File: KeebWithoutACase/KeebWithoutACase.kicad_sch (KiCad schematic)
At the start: 134 parts, among them SW1 SW_Push_45deg, SW10 SW_Push_45deg, SW11 SW_Push_45deg, SW12 SW_Push_45deg, SW13 SW_Push_45deg, SW14 2U, SW15 1.5U, SW16 SW_Push_45deg, SW17 SW_Push_45deg, SW18 SW_Push_45deg, SW19 SW_Push_45deg, SW2 SW_Push_45deg, SW20 SW_Push_45deg, SW21 SW_Push_45deg, SW22 SW_Push_45deg, SW23 SW_Push_45deg, SW24 SW_Push_45deg, SW25 SW_Push_45deg, SW26 SW_Push_45deg, SW27 SW_Push_45deg, SW28 1.5U, SW29 1.75U, SW3 SW_Push_45deg, SW30 2.25U, SW31 SW_Push_45deg, SW32 SW_Push_45deg, SW33 SW_Push_45deg, SW34 SW_Push_45deg, SW35 SW_Push_45deg, SW36 SW_Push_45deg, SW37 SW_Push_45deg, SW38 SW_Push_45deg, SW39 SW_Push_45deg, SW4 SW_Push_45deg, SW40 SW_Push_45deg, SW41 SW_Push_45deg, SW42 SW_Push_45deg, SW43 SW_Push_45deg, SW44 SW_Push_45deg, SW45 SW_Push_45deg, SW46 SW_Push_45deg, SW47 SW_Push_45deg, SW48 SW_Push_45deg, SW49 SW_Push_45deg, SW5 SW_Push_45deg, SW50 SW_Push_45deg, SW51 SW_Push_45deg, SW52 2.75U, SW53 2.25U, SW54 1.25U, SW55 RotaryEncoder, SW56 SW_Push_45deg, SW57 1.25U, SW58 SW_Push_45deg, SW59 SW_Push_45deg, SW6 SW_Push_45deg, SW60 SW_Push_45deg, SW62 1.25U, SW63 SW_Push_45deg, SW64 SW_Push_45deg, SW65 SW_Push_45deg, SW66 SW_Push_45deg, SW67 SW_Push_45deg, SW7 SW_Push_45deg, SW8 SW_Push_45deg, SW9 SW_Push_45deg

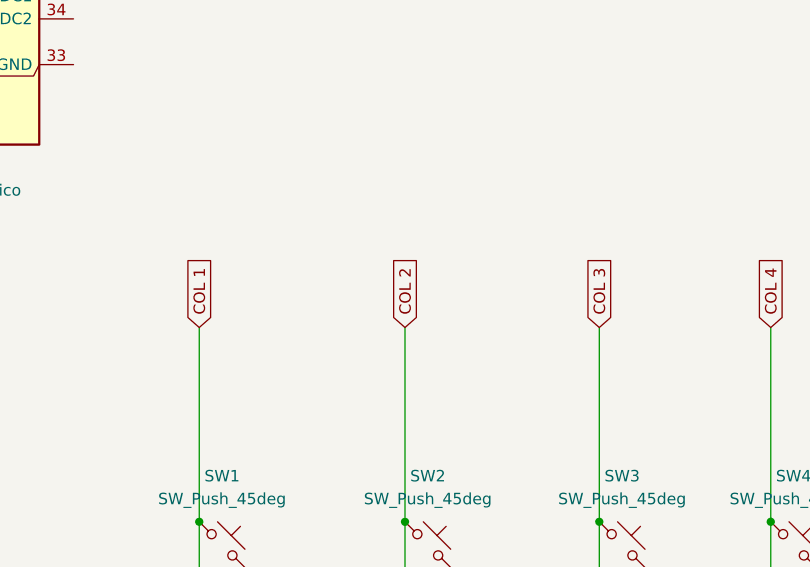
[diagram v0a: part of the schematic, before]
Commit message: this time completed the first row with the correct keys
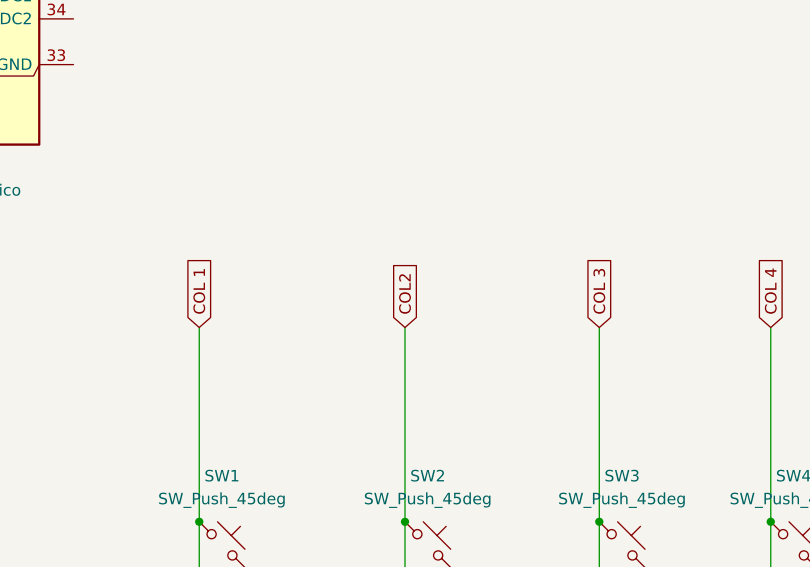
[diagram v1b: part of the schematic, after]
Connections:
- net COL 1: no longer A1.9 (GPIO6)
- new net COL 2: A1.9 (GPIO6)

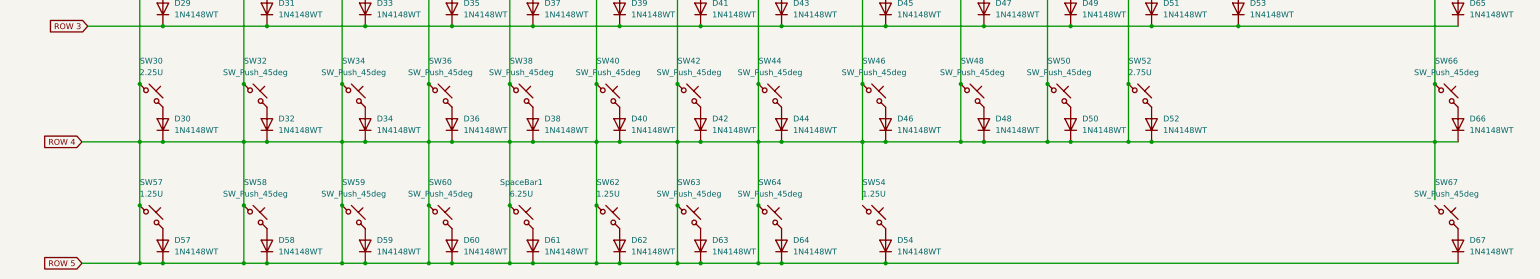
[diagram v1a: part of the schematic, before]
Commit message: fixed the schm col1 bleeding
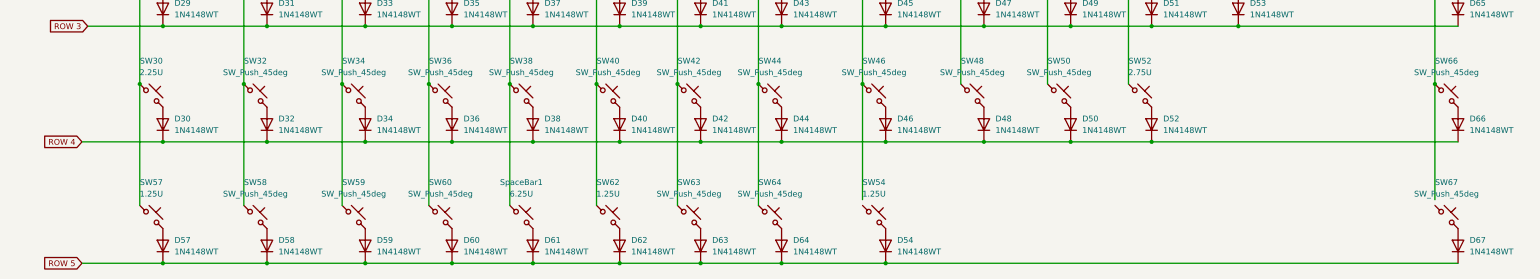
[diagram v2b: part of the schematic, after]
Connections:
- net COL 1: no longer A1.10 (GPIO7), A1.11 (GPIO8), A1.12 (GPIO9), A1.14 (GPIO10), A1.15 (GPIO11), A1.16 (GPIO12), A1.17 (GPIO13), A1.19 (GPIO14), A1.20 (GPIO15), A1.21 (GPIO16), A1.25 (GPIO19), A1.5 (GPIO3), A1.6 (GPIO4), D30.1 (K), D32.1 (K), D34.1 (K), D36.1 (K), D38.1 (K), D40.1 (K), D42.1 (K), D44.1 (K), D46.1 (K), D48.1 (K), D50.1 (K), D52.1 (K), D54.1 (K), D57.1 (K), D58.1 (K), D59.1 (K), D60.1 (K), D61.1 (K), D62.1 (K), D63.1 (K), D64.1 (K), D66.1 (K), D67.1 (K), SW10.1, SW11.1, SW12.1, SW16.1, SW17.1, SW18.1, SW19.1, SW2.1, SW20.1, SW21.1, SW22.1, SW23.1, SW24.1, SW25.1, SW26.1, SW3.1, SW31.1, SW32.1, SW33.1, SW34.1, SW35.1, SW36.1, SW37.1, SW38.1, SW39.1, SW4.1, SW40.1, SW41.1, SW42.1, SW43.1, SW44.1, SW45.1, SW46.1, SW47.1, SW48.1, SW49.1, SW5.1, SW50.1, SW51.1, SW52.1, SW56.1, SW58.1, SW59.1, SW6.1, SW60.1, SW62.1, SW63.1, SW64.1, SW65.1, SW66.1, SW7.1, SW8.1, SW9.1, SpaceBar1.1
- new net COL 10: A1.19 (GPIO14), SW10.1, SW24.1, SW47.1, SW48.1
- new net COL 11: A1.20 (GPIO15), SW11.1, SW25.1, SW49.1, SW50.1
- new net COL 12: A1.21 (GPIO16), SW12.1, SW26.1, SW51.1, SW52.1
- new net COL 15: A1.25 (GPIO19), SW56.1, SW65.1, SW66.1
- new net COL 3: A1.10 (GPIO7), SW17.1, SW3.1, SW33.1, SW34.1, SW59.1
- new net COL 4: A1.11 (GPIO8), SW18.1, SW35.1, SW36.1, SW4.1, SW60.1
- new net COL 5: A1.12 (GPIO9), SW19.1, SW37.1, SW38.1, SW5.1, SpaceBar1.1
- new net COL 6: A1.14 (GPIO10), SW20.1, SW39.1, SW40.1, SW6.1, SW62.1
- new net COL 7: A1.15 (GPIO11), SW21.1, SW41.1, SW42.1, SW63.1, SW7.1
- new net COL 8: A1.16 (GPIO12), SW22.1, SW43.1, SW44.1, SW64.1, SW8.1
- new net COL 9: A1.17 (GPIO13), SW23.1, SW45.1, SW46.1, SW9.1
- new net COL2: SW16.1, SW2.1, SW31.1, SW32.1, SW58.1
- new net ROW 4: A1.5 (GPIO3), D30.1 (K), D32.1 (K), D34.1 (K), D36.1 (K), D38.1 (K), D40.1 (K), D42.1 (K), D44.1 (K), D46.1 (K), D48.1 (K), D50.1 (K), D52.1 (K), D66.1 (K)
- new net ROW 5: A1.6 (GPIO4), D54.1 (K), D57.1 (K), D58.1 (K), D59.1 (K), D60.1 (K), D61.1 (K), D62.1 (K), D63.1 (K), D64.1 (K), D67.1 (K)

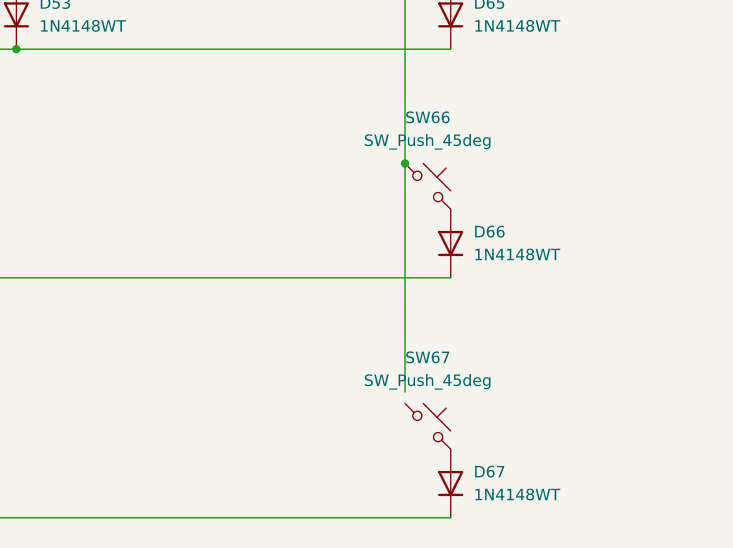
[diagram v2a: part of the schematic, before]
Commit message: fixed wiring the switch matrix
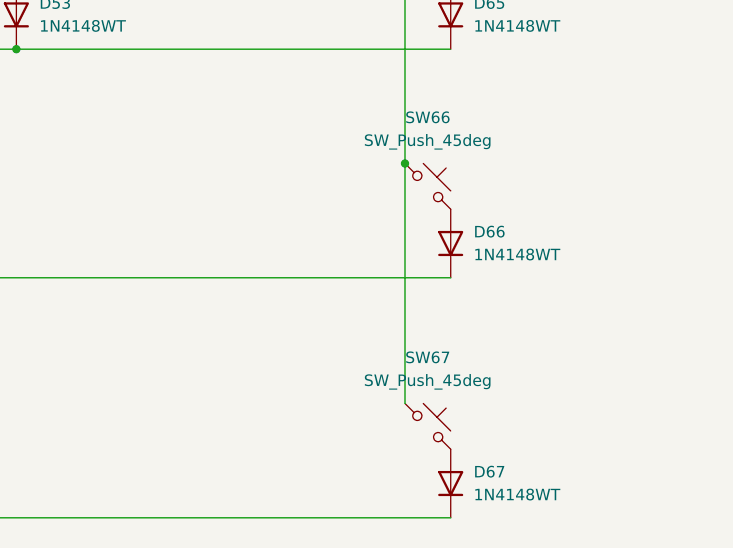
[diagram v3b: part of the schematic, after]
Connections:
- net COL 15: now also SW67.1
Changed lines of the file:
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@@
 	(wire
 		(pts
-			(xy 372.11 208.28) (xy 372.11 233.68)
+			(xy 372.11 208.28) (xy 372.11 234.95)
 		)
 		(stroke

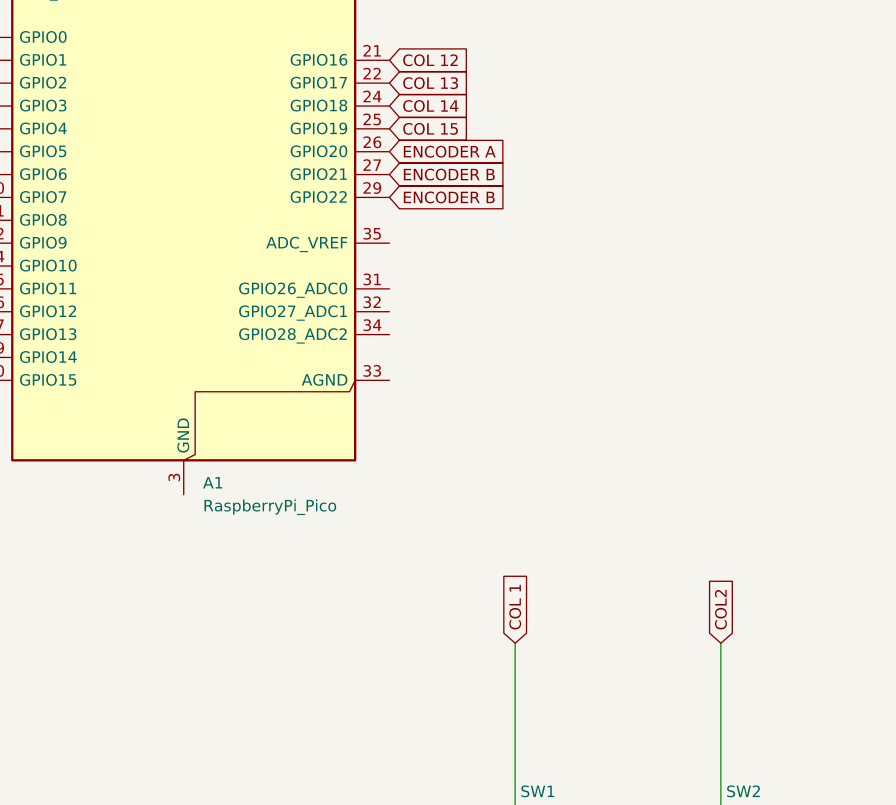
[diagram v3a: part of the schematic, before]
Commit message: wired all the stuff to the mcu and completed the wiring of the pcb for the keyboard
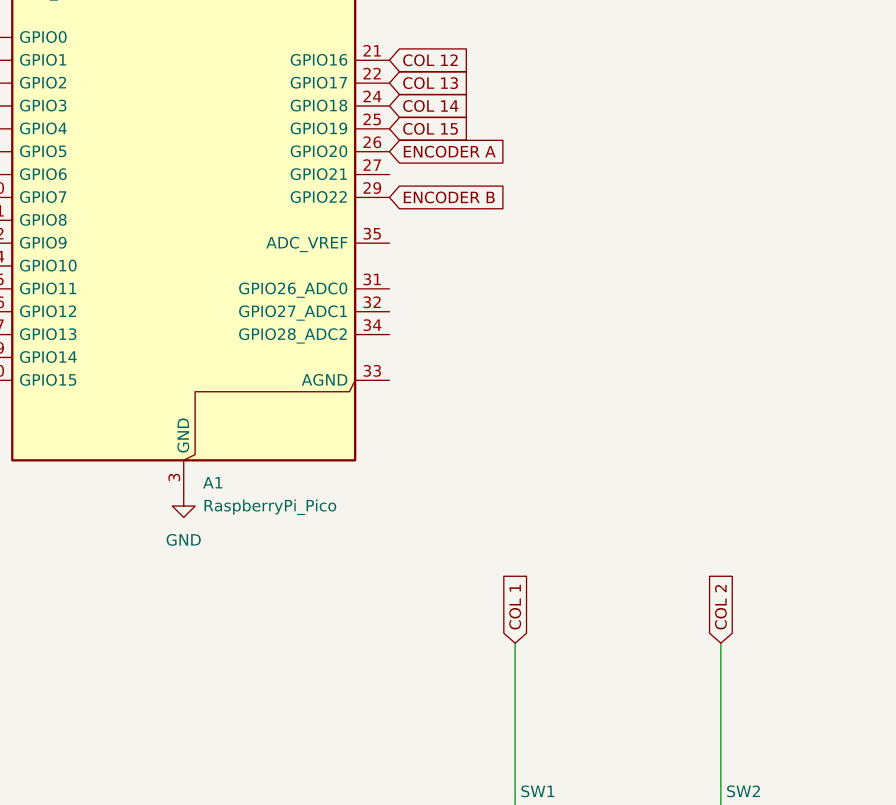
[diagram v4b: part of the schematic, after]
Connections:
- net COL2 is gone; now on net COL 2: SW16.1, SW2.1, SW31.1, SW32.1, SW58.1
- net ENCODER B: no longer A1.27 (GPIO21)
- net GND: now also A1.13 (GND), A1.18 (GND), A1.23 (GND), A1.28 (GND), A1.3 (GND), A1.38 (GND), A1.8 (GND)
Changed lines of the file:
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@@
 		)
 	)
-	(global_label "COL2"
+	(global_label "COL 2"
 		(shape input)
 		(at 110.49 113.03 90)
@@
 		)
 		(property "Intersheetrefs" "${INTERSHEET_REFS}"
-			(at 110.49 105.2067 90)
+			(at 110.49 104.2391 90)
 			(effects
 				(font
@@
 		)
 	)
-	(global_label "ENCODER B"
-		(shape input)
-		(at 73.66 63.5 0)
-		(fields_autoplaced yes)
-		(effects
-			(font
-				(size 1.27 1.27)
-			)
-			(justify left)
-		)
-		(property "Intersheetrefs" "${INTERSHEET_REFS}"
-			(at 87.6518 63.5 0)
-			(effects
-				(font
-					(size 1.27 1.27)
-				)
-				(justify left)
-				(hide yes)
-			)
-		)
-	)
 	(global_label "COL 12"
 		(shape input)
@@
 		)
 	)
+	(global_label "ENCODER B"
+		(shape input)
+		(at 73.66 63.5 0)
+		(fields_autoplaced yes)
+		(effects
+			(font
+				(size 1.27 1.27)
+			)
+			(justify left)
+		)
+		(property "Intersheetrefs" "${INTERSHEET_REFS}"
+			(at 87.6518 63.5 0)
+			(effects
+				(font
+					(size 1.27 1.27)
+				)
+				(justify left)
+				(hide yes)
+			)
+		)
+	)
 	(global_label "COL 4"
 		(shape input)
@@
 		)
 	)
-	(global_label "ENCODER B"
-		(shape input)
-		(at 73.66 60.96 0)
-		(fields_autoplaced yes)
-		(effects
-			(font
-				(size 1.27 1.27)
-			)
-			(justify left)
-		)
-		(property "Intersheetrefs" "${INTERSHEET_REFS}"
-			(at 87.6518 60.96 0)
-			(effects
-				(font
-					(size 1.27 1.27)
-				)
-				(justify left)
-				(hide yes)
-			)
-		)
-	)
 	(global_label "COL 5"
 		(shape input)
@@
 					(unit 1)
 				)
+			)
+		)
+	)
+	(symbol
+		(lib_id "power:GND")
+		(at 50.8 96.52 0)
+		(unit 1)
+		(exclude_from_sim no)
+		(in_bom yes)
+		(on_board yes)
+		(dnp no)
+		(fields_autoplaced yes)
+		(property "Reference" "#PWR02"
+			(at 50.8 102.87 0)
+			(effects
+				(font
+					(size 1.27 1.27)
+				)
+				(hide yes)
+			)
+		)
+		(property "Value" "GND"
+			(at 50.8 101.6 0)
+			(effects
+				(font
+					(size 1.27 1.27)
+				)
+			)
+		)
+		(property "Footprint" ""
+			(at 50.8 96.52 0)
+			(effects
+				(font
+					(size 1.27 1.27)
+				)
+				(hide yes)
+			)
+		)
+		(property "Datasheet" ""
+			(at 50.8 96.52 0)
+			(effects
+				(font
+					(size 1.27 1.27)
+				)
+				(hide yes)
+			)
+		)
+		(property "Description" "Power symbol creates a global label with name \"GND\" , ground"
+			(at 50.8 96.52 0)
+			(effects
+				(font
+					(size 1.27 1.27)
+				)
+				(hide yes)
+			)
+		)
+		(pin "1"
+		)
+		(instances
+			(project ""
+				(path "/35878fee-9f0f-4654-b50b-b205a4b1f30d"
+					(reference "#PWR02")
+					(unit 1)
+				)
